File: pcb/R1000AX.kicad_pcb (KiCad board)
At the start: 4 copper layers, 175 x 68.5 mm, 146 parts, among them J1 PCIESOCKET-X1, J10 PCIESOCKET-X1, J11 PCIESOCKET-X1, J12 PCIESOCKET-X1, J13 PCIESOCKET-X1, J14 PCIESOCKET-X1, J15 PCIESOCKET-X1, J16 CONN127P-02X05, J17 USB_B_RECEPTACLE, J18 SOCKET254P-01X02, J19 COMPUTE_MOD_1, J2 PCIESOCKET-X1, J20 USB_A_RECEPTACLE, J25 SOCKET420P-02X04-CPU, J3 PCIESOCKET-X1, J31 USB_A_RECEPTACLE, J4 PCIESOCKET-X1, J5 PCIESOCKET-X1, J6 PCIESOCKET-X1, J7 PCIESOCKET-X1, J8 PCIESOCKET-X1, J81 SOCKET254P-01X02, J82 SOCKET254P-01X02, J83 SOCKET254P-01X02, J9 PCIESOCKET-X1, Q1 DMG2305UX-7, Q2 PSMN1R2-30YLC, Q3 Q_PNP_BEC, Q4 Q_NPN_BEC, Q5 Q_PNP_BEC, Q6 Q_PNP_BEC, U1 LPC1769FBD100,551, U2 AP3418, U20 M24C08-FDW6TP, U3 BD9E302EFJ-E2, U4 INA3221AIRGVR, U5 LM5060MM/NOPB, Y1 XTAL4_12MHz

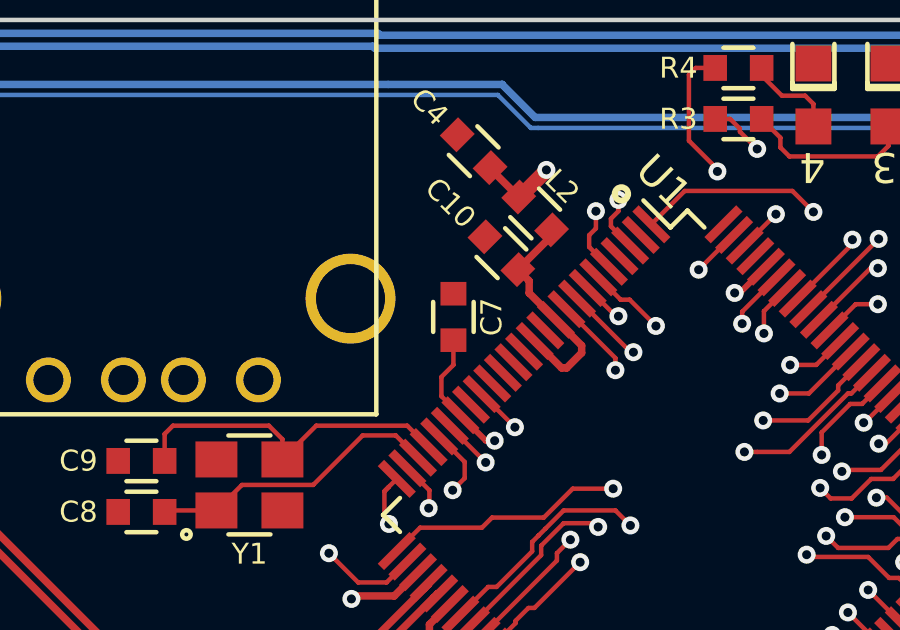
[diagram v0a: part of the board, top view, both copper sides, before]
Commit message: fixed c7 location
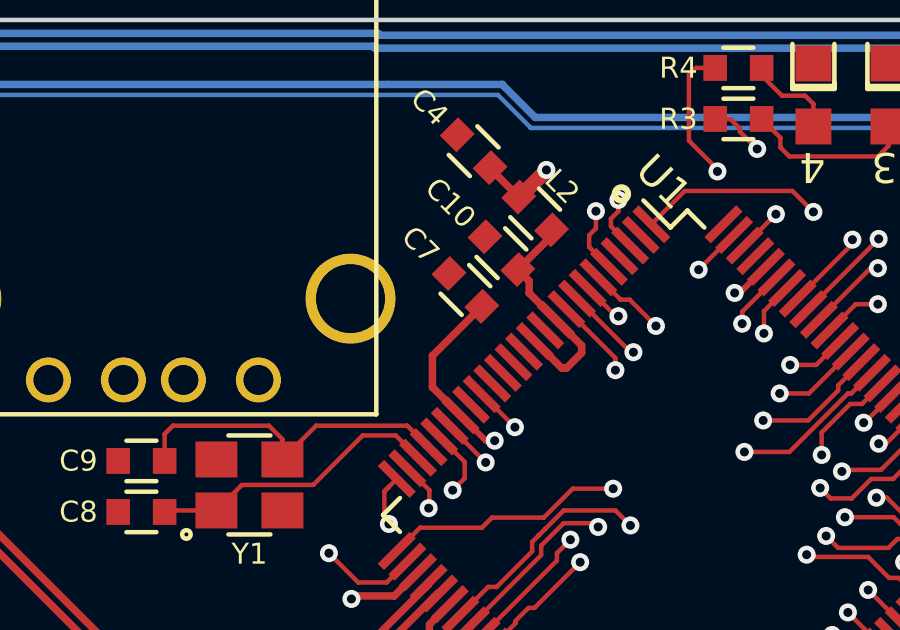
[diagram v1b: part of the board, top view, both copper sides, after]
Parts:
- moved C7 0.98 mm to (107.6, 82.5), turned to 135 degrees
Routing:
- net +3V3: track 55.7 -> 57.4 mm
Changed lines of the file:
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@@
     (thickness 1.6)
     (drawings 72)
-    (tracks 3410)
+    (tracks 3409)
     (zones 0)
     (modules 146)
@@
   (page A4)
   (layers
-    (0 F.Cu signal hide)
-    (1 In1.Cu signal hide)
+    (0 F.Cu signal)
+    (1 In1.Cu signal)
     (2 In2.Cu signal hide)
     (31 B.Cu signal hide)
@@
   )
   (setup
-    (last_trace_width 0.15)
+    (last_trace_width 0.25)
     (user_trace_width 0.2)
     (user_trace_width 0.25)
@@
   )
   (module Main:CAPC0603 (layer F.Cu)
-    (at 107.2 83.4 90)
+    (at 107.6 82.5 135)
     (descr "Resistor SMD 0603, reflow soldering, Vishay (see dcrcw.pdf)")
     (tags "resistor 0603")
     (attr smd)
-    (fp_text reference C7 (at 0 1.272792 90) (layer F.SilkS)
+    (fp_text reference C7 (at 2.12132 0 135) (layer F.SilkS)
       (effects (font (size 0.7 0.7) (thickness 0.15)))
     )
-    (fp_text value CC0603KRX7R9BB104 (at 0 0.508 90) (layer F.Fab)
+    (fp_text value CC0603KRX7R9BB104 (at 0 0.508 135) (layer F.Fab)
       (effects (font (size 0.127 0.127) (thickness 0.03)))
     )
@@
     (fp_line (start 0.5 0.675) (end -0.5 0.675) (layer F.SilkS) (width 0.15))
     (fp_line (start -0.5 -0.675) (end 0.5 -0.675) (layer F.SilkS) (width 0.15))
-    (pad 1 smd rect (at -0.7745 0 90) (size 0.787 0.864) (layers F.Cu F.Paste F.Mask)
+    (pad 1 smd rect (at -0.7745 0 135) (size 0.787 0.864) (layers F.Cu F.Paste F.Mask)
       (net 1 +3V3))
-    (pad 2 smd rect (at 0.7745 0 90) (size 0.787 0.864) (layers F.Cu F.Paste F.Mask)
+    (pad 2 smd rect (at 0.7745 0 135) (size 0.787 0.864) (layers F.Cu F.Paste F.Mask)
       (net 2 GND))
     (model main.3dshapes/CAPC0603.wrl
@@
   (gr_arc (start 53 140) (end 53 142) (angle 90) (layer Edge.Cuts) (width 0.15))
   (gr_line (start 51 75.5) (end 51 140) (angle 90) (layer Edge.Cuts) (width 0.15))
+  (segment (start 108.147654 83.047654) (end 106.5 84.695308) (width 0.25) (layer F.Cu) (net 1))
+  (segment (start 106.5 85.742641) (end 107.433957 86.676598) (width 0.25) (layer F.Cu) (net 1))
+  (segment (start 106.5 84.695308) (end 106.5 85.742641) (width 0.25) (layer F.Cu) (net 1))
   (segment (start 188.8255 97.4) (end 188.8255 95.6) (width 0.15) (layer F.Cu) (net 1))
   (segment (start 188.8255 95.6) (end 188.8 95.5745) (width 0.15) (layer F.Cu) (net 1))
@@
   (via (at 108.575 87.525) (size 0.6) (drill 0.3) (layers F.Cu B.Cu) (net 1))
   (segment (start 108.282359 87.525) (end 108.575 87.525) (width 0.2) (layer F.Cu) (net 1))
-  (segment (start 107.433957 86.676598) (end 106.8 86.042641) (width 0.15) (layer F.Cu) (net 1))
-  (segment (start 107.2 85) (end 107.2 84.1745) (width 0.15) (layer F.Cu) (net 1))
-  (segment (start 106.8 85.4) (end 107.2 85) (width 0.15) (layer F.Cu) (net 1))
-  (segment (start 106.8 86.042641) (end 106.8 85.4) (width 0.15) (layer F.Cu) (net 1))
   (segment (start 117.616295 81.726851) (end 116.743146 82.6) (width 0.2) (layer F.Cu) (net 1))
   (via (at 116.575 82.6) (size 0.6) (drill 0.3) (layers F.Cu B.Cu) (net 1))
